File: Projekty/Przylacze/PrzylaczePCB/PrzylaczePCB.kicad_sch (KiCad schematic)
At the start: 38 parts, among them J1 Conn_02x04_Odd_Even, J2 Conn_02x20_Odd_Even, J3 Conn_01x06, J4 USB_B, J5 Screw_Terminal_01x06, Q1 BC557, Q2 BC547, Q3 BC557, Q4 BC547, Q5 2N3904, Q6 2N3904, Q7 BC557, Q8 BC557, SW1 SW_Push, U1 74AHC1G04, U10 LDL1117S33R, U2 74AHC1G04, U3 ATSAM4S2AA-AU, U9 DI78M05UAB

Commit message: Przyłącze - projekt PCB v0.5
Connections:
- net RX/TX ENABLE  is gone; now on net RX/TX ENABLE: U3.28 (PA4/PGMNCMD)
- net A: now also J2.33 (Pin_33), J2.34 (Pin_34); no longer J2.1 (Pin_1), J2.2 (Pin_2)
- net B: now also J2.35 (Pin_35), J2.36 (Pin_36); no longer J2.3 (Pin_3), J2.4 (Pin_4)
- net CANH: now also J2.39 (Pin_39), J2.40 (Pin_40); no longer J2.5 (Pin_5), J2.6 (Pin_6)
- net CANL: now also J2.37 (Pin_37), J2.38 (Pin_38); no longer J2.7 (Pin_7), J2.8 (Pin_8)
- net CS0: now also J2.7 (Pin_7); no longer J2.36 (Pin_36)
- net CS3: now also J2.5 (Pin_5); no longer J2.34 (Pin_34)
- net EN: now also J2.28 (Pin_28); no longer J2.17 (Pin_17)
- net ERR: now also J2.30 (Pin_30); no longer J2.19 (Pin_19)
- net GND: no longer U3.34 (GND)
- net INT: now also J2.25 (Pin_25); no longer J2.33 (Pin_33)
- net MISO: now also J2.8 (Pin_8); no longer J2.30 (Pin_30)
- net MOSI: now also J2.6 (Pin_6); no longer J2.28 (Pin_28)
- net OPTO_R1: now also J2.1 (Pin_1); no longer J2.20 (Pin_20)
- net OPTO_R2: now also J2.3 (Pin_3); no longer J2.22 (Pin_22)
- net OPTO_SW1: now also J2.2 (Pin_2); no longer J2.16 (Pin_16)
- net OPTO_SW2: now also J2.4 (Pin_4); no longer J2.18 (Pin_18)
- net RESET: now also J2.27 (Pin_27); no longer J2.35 (Pin_35)
- net RX0BF: now also J2.19 (Pin_19); no longer J2.27 (Pin_27)
- net RX1BF: now also J2.21 (Pin_21); no longer J2.29 (Pin_29)
- net RXD: now also J2.22 (Pin_22); no longer J2.11 (Pin_11)
- net RX_MCU: now also J2.16 (Pin_16); no longer J2.12 (Pin_12)
- net RX/TX ENABLE: now also J2.18 (Pin_18); no longer J2.14 (Pin_14)
- net SOF: now also J2.23 (Pin_23); no longer J2.31 (Pin_31)
- net SPCK: now also J2.10 (Pin_10); no longer J2.32 (Pin_32)
- net STB_FT: now also J2.24 (Pin_24); no longer J2.13 (Pin_13)
- net TX0RTS: now also J2.13 (Pin_13); no longer J2.21 (Pin_21)
- net TX1RTS: now also J2.15 (Pin_15); no longer J2.23 (Pin_23)
- net TX2RTS: now also J2.17 (Pin_17); no longer J2.25 (Pin_25)
- net TXD: now also J2.20 (Pin_20); no longer J2.9 (Pin_9)
- net TX_MCU: now also J2.14 (Pin_14); no longer J2.10 (Pin_10)
- net UART0_RX: now also J2.12 (Pin_12); no longer J2.24 (Pin_24)
- net UART0_TX: now also J2.11 (Pin_11); no longer J2.26 (Pin_26)
- net WAKE: now also J2.26 (Pin_26); no longer J2.15 (Pin_15)
- no-connect marks 23 -> 20

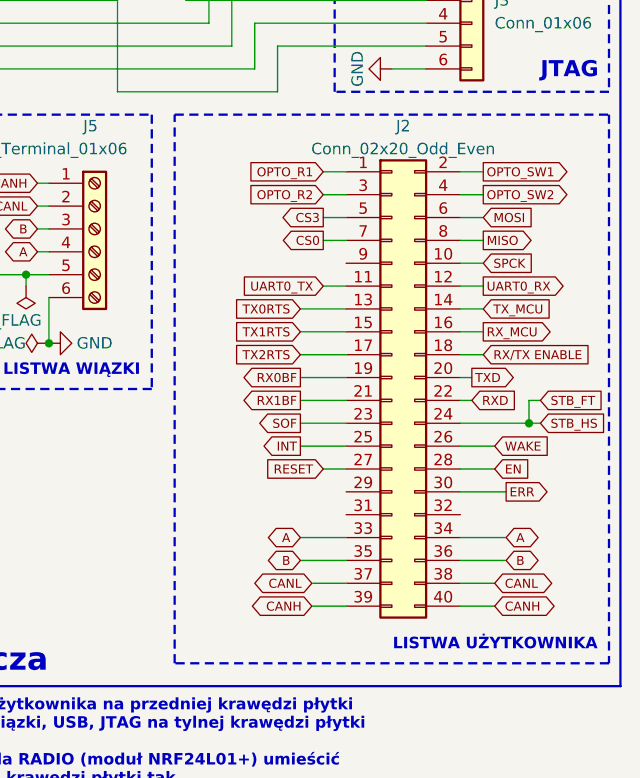
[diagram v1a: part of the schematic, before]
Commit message: Przyłącze - projekt PCB v1.0
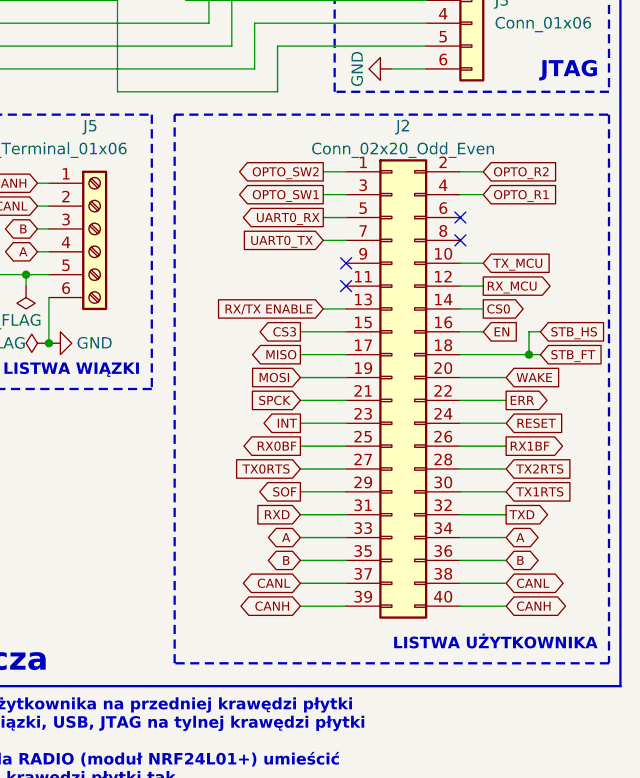
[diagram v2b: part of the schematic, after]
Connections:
- net CS0: now also J2.14 (Pin_14); no longer J2.7 (Pin_7)
- net CS3: now also J2.15 (Pin_15); no longer J2.5 (Pin_5)
- net EN: now also J2.16 (Pin_16); no longer J2.28 (Pin_28)
- net ERR: now also J2.22 (Pin_22); no longer J2.30 (Pin_30)
- net INT: now also J2.23 (Pin_23); no longer J2.25 (Pin_25)
- net MISO: now also J2.17 (Pin_17); no longer J2.8 (Pin_8)
- net MOSI: now also J2.19 (Pin_19); no longer J2.6 (Pin_6)
- net OPTO_R1: now also J2.4 (Pin_4); no longer J2.1 (Pin_1)
- net OPTO_R2: now also J2.2 (Pin_2); no longer J2.3 (Pin_3)
- net OPTO_SW1: now also J2.3 (Pin_3); no longer J2.2 (Pin_2)
- net OPTO_SW2: now also J2.1 (Pin_1); no longer J2.4 (Pin_4)
- net RESET: now also J2.24 (Pin_24); no longer J2.27 (Pin_27)
- net RX0BF: now also J2.25 (Pin_25); no longer J2.19 (Pin_19)
- net RX1BF: now also J2.26 (Pin_26); no longer J2.21 (Pin_21)
- net RXD: now also J2.31 (Pin_31); no longer J2.22 (Pin_22)
- net RX_MCU: now also J2.12 (Pin_12); no longer J2.16 (Pin_16)
- net RX/TX ENABLE: now also J2.13 (Pin_13); no longer J2.18 (Pin_18)
- net SOF: now also J2.29 (Pin_29); no longer J2.23 (Pin_23)
- net SPCK: now also J2.21 (Pin_21); no longer J2.10 (Pin_10)
- net STB_FT: now also J2.18 (Pin_18); no longer J2.24 (Pin_24)
- net TX0RTS: now also J2.27 (Pin_27); no longer J2.13 (Pin_13)
- net TX1RTS: now also J2.30 (Pin_30); no longer J2.15 (Pin_15)
- net TX2RTS: now also J2.28 (Pin_28); no longer J2.17 (Pin_17)
- net TXD: now also J2.32 (Pin_32); no longer J2.20 (Pin_20)
- net TX_MCU: now also J2.10 (Pin_10); no longer J2.14 (Pin_14)
- net UART0_RX: now also J2.5 (Pin_5); no longer J2.12 (Pin_12)
- net UART0_TX: now also J2.7 (Pin_7); no longer J2.11 (Pin_11)
- net WAKE: now also J2.20 (Pin_20); no longer J2.26 (Pin_26)
- no-connect marks 20 -> 24

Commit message: Przyłącze - projekt PCB v1.1
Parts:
- added C22: 330n, Capacitor_THT:C_Disc_D5.0mm_W2.5mm_P2.50mm, symbol Device:C_Small
- added C23: 100n, Capacitor_THT:C_Disc_D5.0mm_W2.5mm_P2.50mm, symbol Device:C_Small
- added C24: 1u, Capacitor_THT:CP_Radial_D5.0mm_P2.00mm, symbol Device:C_Polarized_Small_US
- added C25: 4.7u, Capacitor_THT:CP_Radial_D5.0mm_P2.00mm, symbol Device:C_Polarized_Small_US
- added C3 (x7): 100n, Capacitor_THT:C_Disc_D5.0mm_W2.5mm_P2.50mm, symbol Device:C
- added L1: 10u, Inductor_SMD:L_1206_3216Metric_Pad1.22x1.90mm_HandSolder, symbol Device:L
- Q10: renamed from Q7; footprint Package_TO_SOT_THT:TO-92_Inline -> Package_TO_SOT_THT:TO-92L_HandSolder
- Q11: renamed from Q5; footprint Package_TO_SOT_THT:TO-92_Inline -> Package_TO_SOT_THT:TO-92L_HandSolder
- Q3: renamed from Q4; footprint Package_TO_SOT_THT:TO-92_Inline -> Package_TO_SOT_THT:TO-92L_HandSolder
- Q4: renamed from Q3; footprint Package_TO_SOT_THT:TO-92_Inline -> Package_TO_SOT_THT:TO-92L_HandSolder
- Q5: renamed from Q6; footprint Package_TO_SOT_THT:TO-92_Inline -> Package_TO_SOT_THT:TO-92L_HandSolder
- Q6: renamed from Q8; footprint Package_TO_SOT_THT:TO-92_Inline -> Package_TO_SOT_THT:TO-92L_HandSolder
- Q8: renamed from Q2; footprint Package_TO_SOT_THT:TO-92_Inline -> Package_TO_SOT_THT:TO-92L_HandSolder
- Q9: renamed from Q1; footprint Package_TO_SOT_THT:TO-92_Inline -> Package_TO_SOT_THT:TO-92L_HandSolder
- renumbered C2 to C1, C3 to C19, C1 to C21, D2 to D10, D1 to D12, J2 to J1, J4 to J2, J1 to J4, R11 to R1, R13 to R2, R2 to R22, R4 to R23, R6 to R24, R10 to R25, R8 to R26, R1 to R34, R3 to R35, R5 to R36, R7 to R37, R9 to R38, R14 to R4, R12 to R5, U3 to U2, U2 to U6, U10 to U7, U9 to U8, U1 to U9
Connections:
- net +12V: now also C22.2, C24.1
- net +3.3V: now also U2.33 (VDDIO), U2.47 (VDDIO), C25.1, C3.1, C3.1, C3.1, C3.1
- net +5V: now also C23.1
- net GND: now also U2.34 (GND), C22.1, C23.2, C24.2, C25.2, C3.2, C3.2, C3.2, C3.2, C3.2, C3.2, C3.2
- net at C19.1, U2.18 (VDDCORE), U2.8 (VDDOUT): now also U2.41 (VDDCORE), C3.1, C3.1, L1.1; no longer U2.48 (VDDPLL)
- new net: C3.1, L1.2, U2.48 (VDDPLL)
- no-connect marks 24 -> 20
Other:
- moved on the sheet: U7, U8

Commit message: Przyłącze - schemat elektryczny v1.3
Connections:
- net GND: now also J1.10 (Pin_10), J1.6 (Pin_6), J1.8 (Pin_8), J1.9 (Pin_9), J2.4 (GND), J2.5 (Shield)
- net TX_MCU: now also J1.11 (Pin_11); no longer J1.10 (Pin_10)
- no-connect marks 20 -> 14

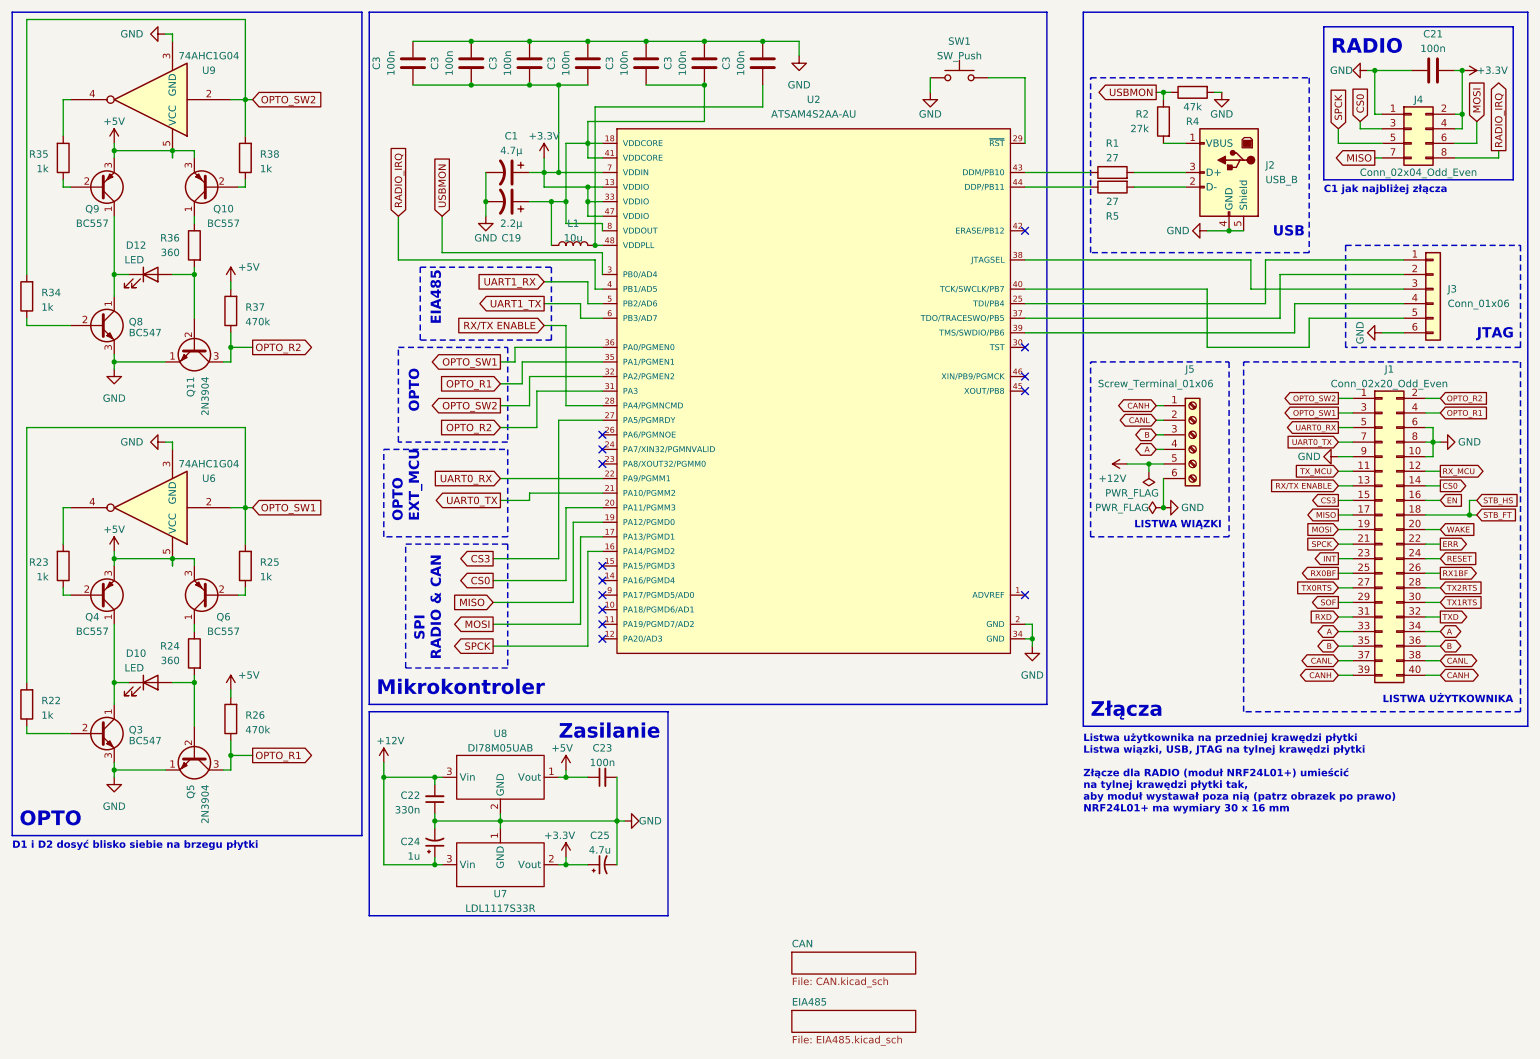
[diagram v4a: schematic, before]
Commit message: Przyłącze - projekt PCB v1.5
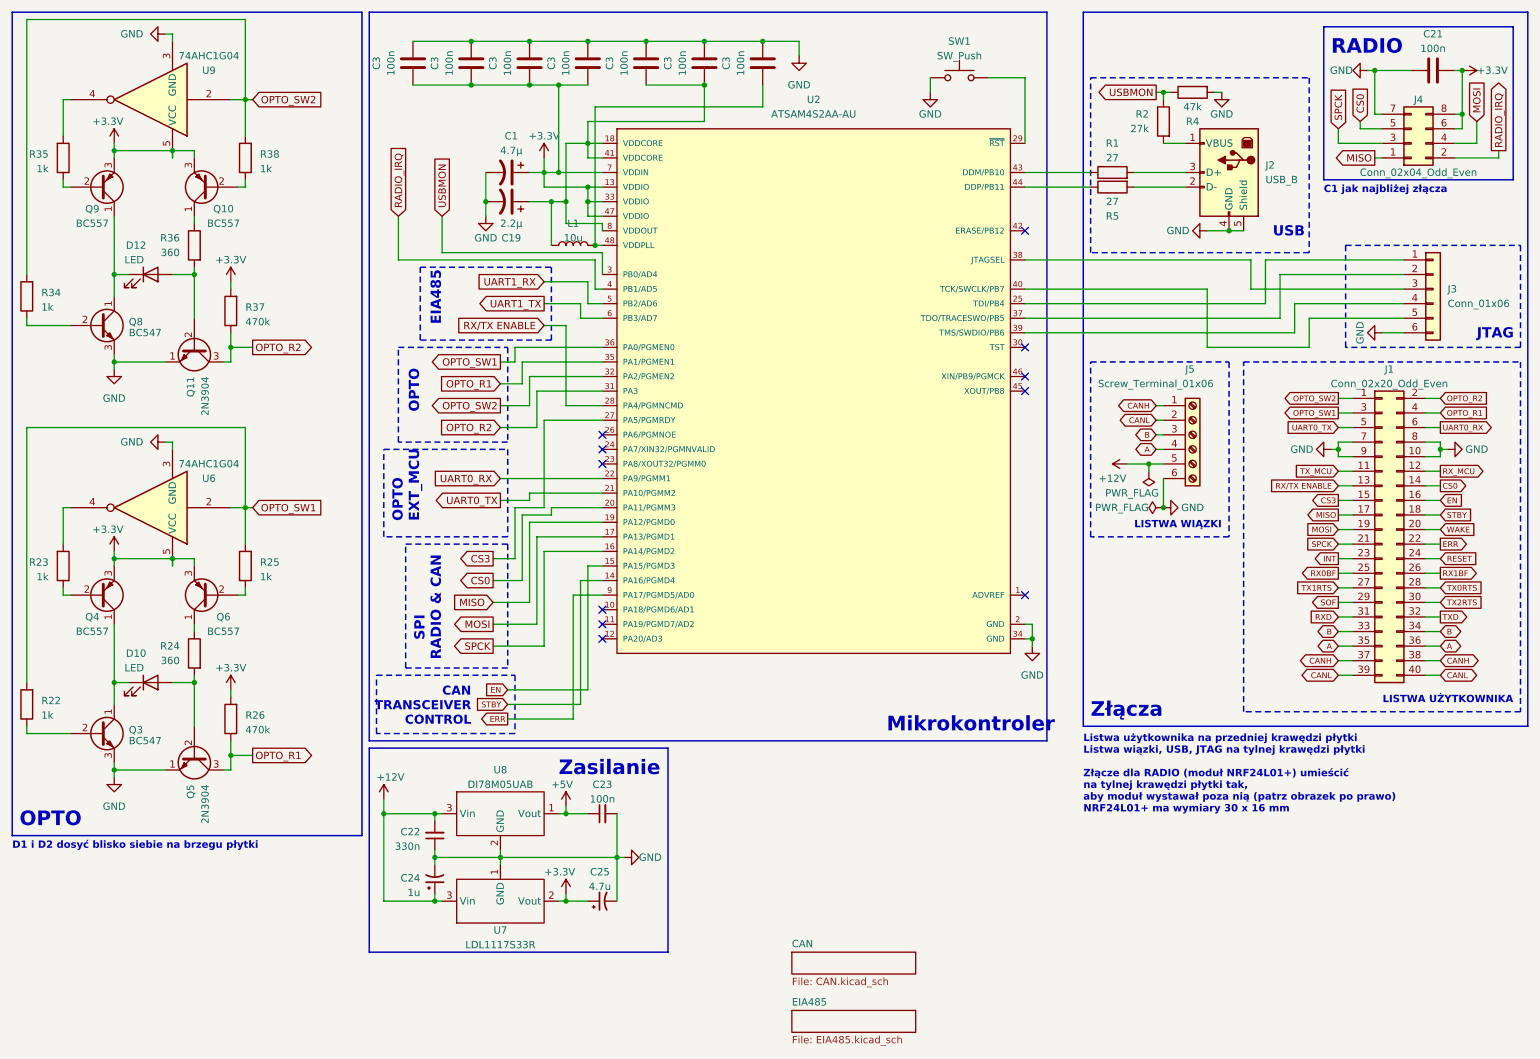
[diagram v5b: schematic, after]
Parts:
- D10, D12: footprint LED_SMD:LED_Kingbright_AAA3528ESGCT -> TestPoint:TestPoint_2Pads_Pitch2.54mm_Drill0.8mm
- J4: footprint Connector_PinHeader_2.54mm:PinHeader_2x04_P2.54mm_Vertical -> Connector_PinSocket_2.54mm:PinSocket_2x04_P2.54mm_Vertical
- Q10, Q11, Q3, Q4, Q5, Q6, Q8, Q9: footprint Package_TO_SOT_THT:TO-92L_HandSolder -> Package_TO_SOT_THT:TO-92L
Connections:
- net STB_FT is gone; now on net STBY: J1.18 (Pin_18)
- net +3.3V: now also J4.6 (Pin_6), J4.8 (Pin_8), Q10.3 (E), Q4.3 (E), Q6.3 (E), Q9.3 (E), R26.2, R37.2, U6.5 (VCC), U9.5 (VCC); no longer J4.2 (Pin_2), J4.4 (Pin_4)
- net +5V: no longer Q10.3 (E), Q4.3 (E), Q6.3 (E), Q9.3 (E), R26.2, R37.2, U6.5 (VCC), U9.5 (VCC)
- net A: now also J1.35 (Pin_35), J1.36 (Pin_36); no longer J1.33 (Pin_33), J1.34 (Pin_34)
- net B: now also J1.33 (Pin_33), J1.34 (Pin_34); no longer J1.35 (Pin_35), J1.36 (Pin_36)
- net CANH: now also J1.37 (Pin_37), J1.38 (Pin_38); no longer J1.39 (Pin_39), J1.40 (Pin_40)
- net CANL: now also J1.39 (Pin_39), J1.40 (Pin_40); no longer J1.37 (Pin_37), J1.38 (Pin_38)
- net CS0: now also J4.5 (Pin_5); no longer J4.3 (Pin_3)
- net EN: now also U2.15 (PA15/PGMD3)
- net ERR: now also U2.9 (PA17/PGMD5/AD0)
- net GND: now also J1.7 (Pin_7), J4.7 (Pin_7); no longer J1.6 (Pin_6), J4.1 (Pin_1)
- net MISO: now also J4.1 (Pin_1); no longer J4.7 (Pin_7)
- net MOSI: now also J4.4 (Pin_4); no longer J4.6 (Pin_6)
- net RADIO_IRQ: now also J4.2 (Pin_2); no longer J4.8 (Pin_8)
- net SPCK: now also J4.3 (Pin_3); no longer J4.5 (Pin_5)
- net TX0RTS: now also J1.28 (Pin_28); no longer J1.27 (Pin_27)
- net TX1RTS: now also J1.27 (Pin_27); no longer J1.30 (Pin_30)
- net TX2RTS: now also J1.30 (Pin_30); no longer J1.28 (Pin_28)
- net UART0_RX: now also J1.6 (Pin_6); no longer J1.5 (Pin_5)
- net UART0_TX: now also J1.5 (Pin_5); no longer J1.7 (Pin_7)
- net STBY: now reaches U2.14 (PA16/PGMD4)
- no-connect marks 14 -> 11
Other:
- note added: "CAN TRANSCEIVER CONTROL"
- moved on the sheet: C22, C23, C24, C25, U7, U8
